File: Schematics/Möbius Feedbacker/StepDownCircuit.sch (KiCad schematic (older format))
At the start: 16 parts

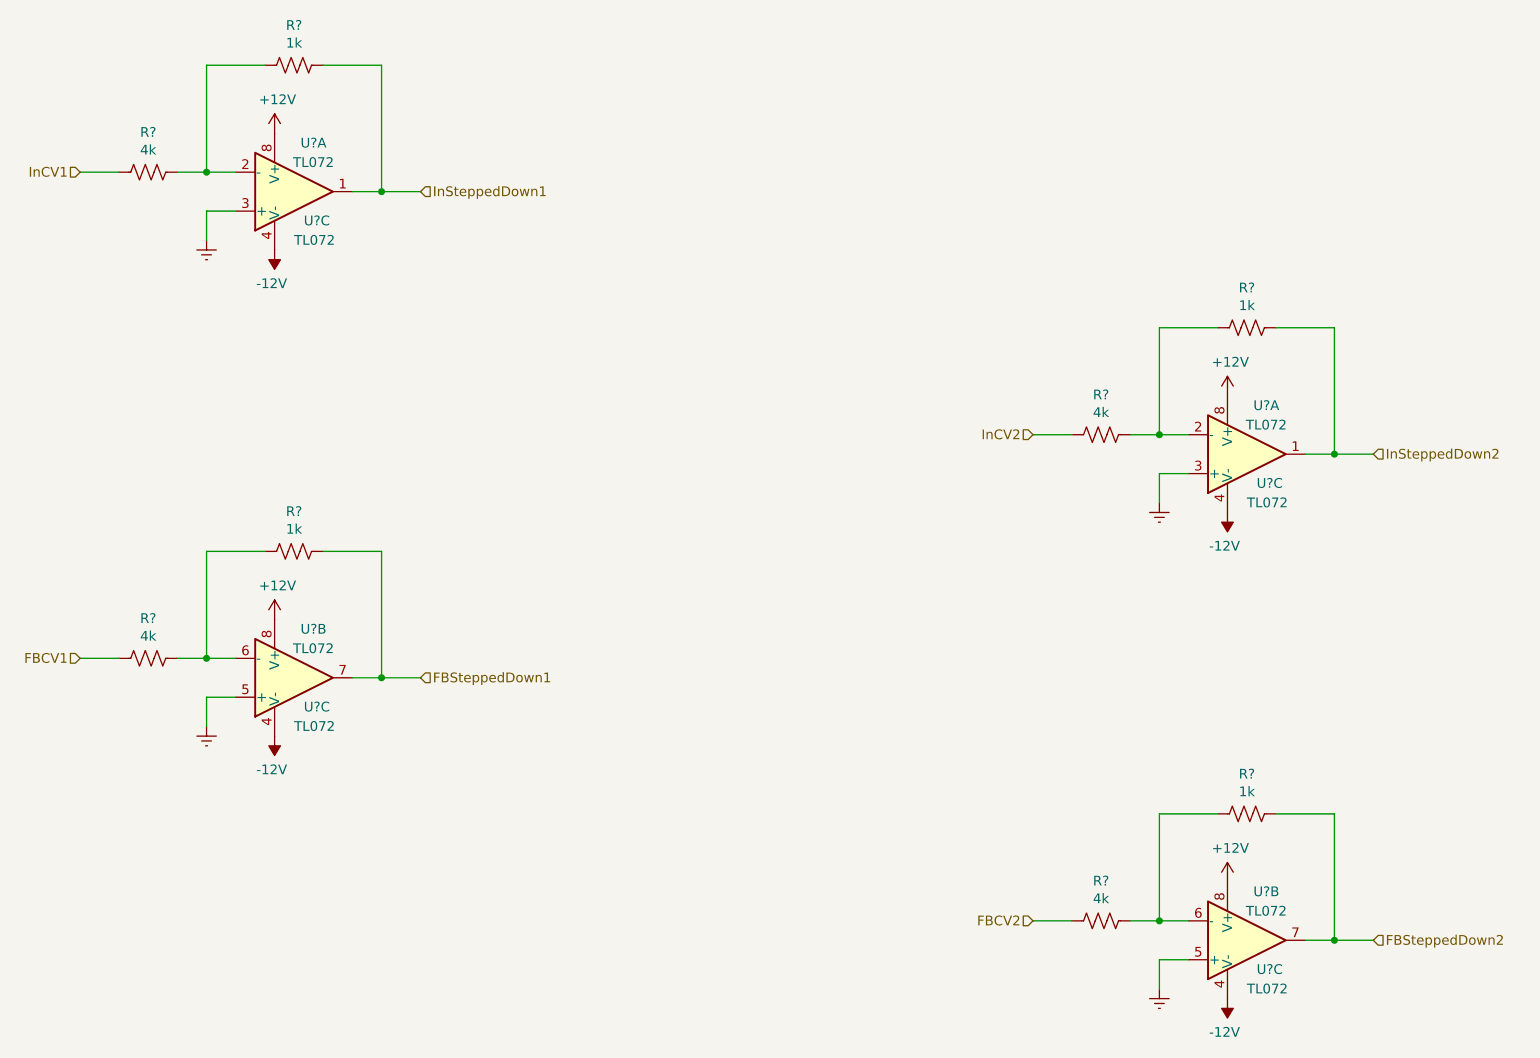
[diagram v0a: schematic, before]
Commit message: Add schematic pdfs, change name to Pathway, update README
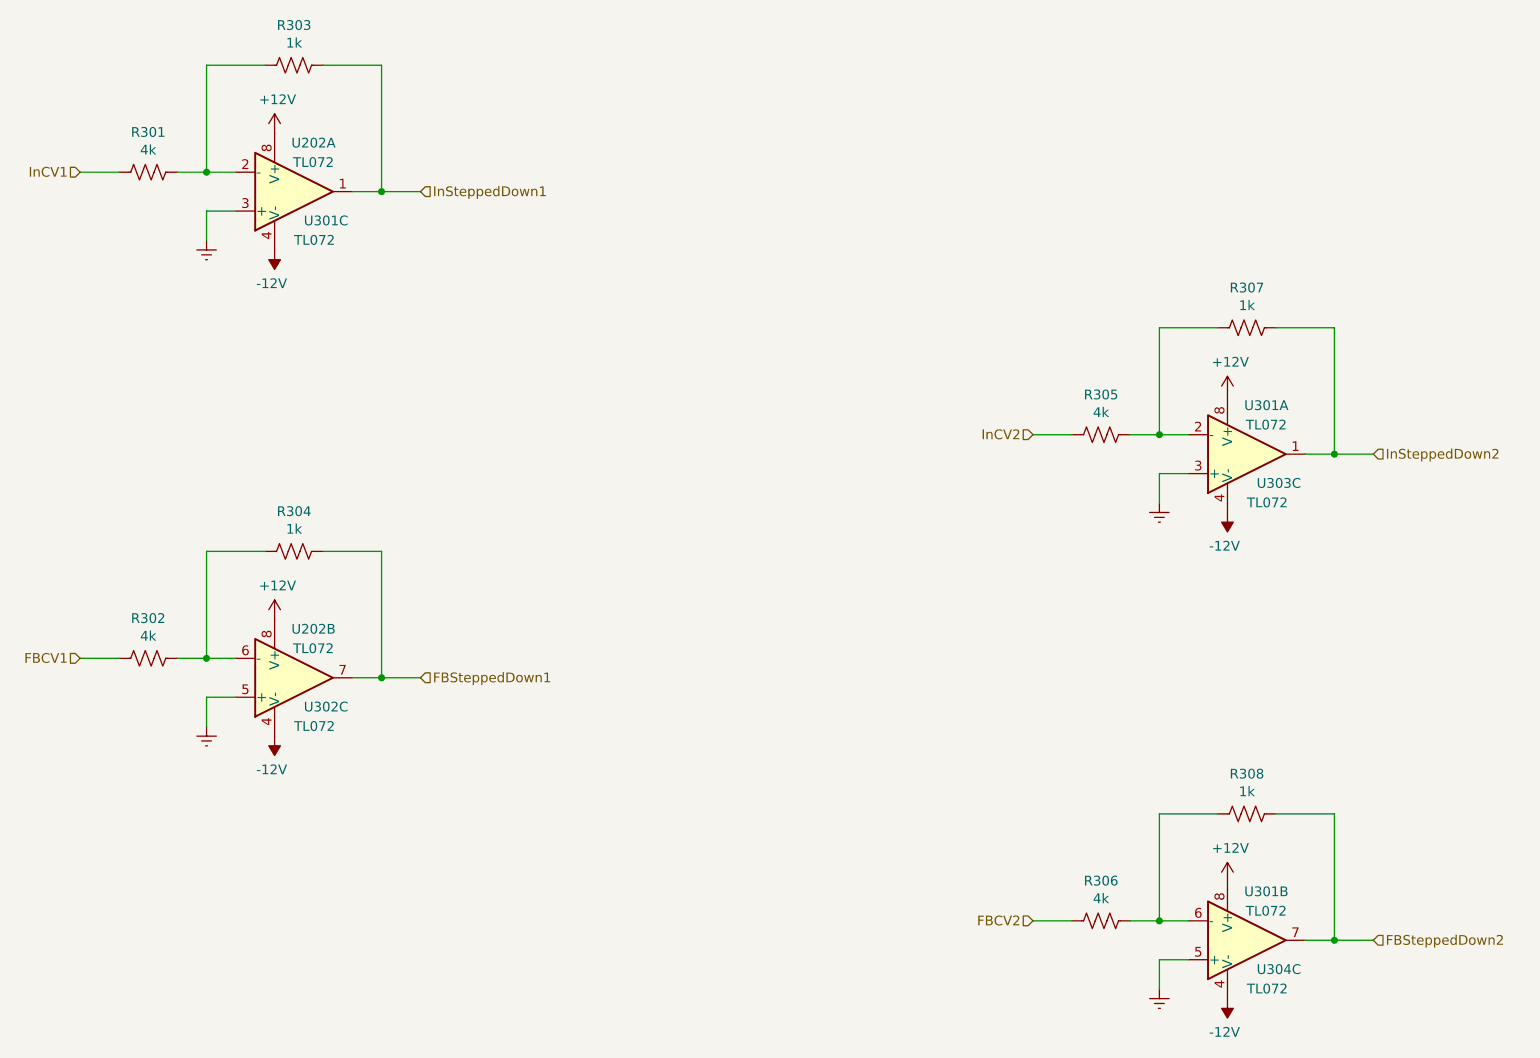
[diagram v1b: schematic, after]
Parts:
- gave numbers to parts that had none: 13
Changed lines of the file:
@@
 $Descr A4 11693 8268
 encoding utf-8
-Sheet 5 4
+Sheet 2 4
 Title ""
 Date ""
@@
 FBSteppedDown1
 $Comp
-L Amplifier_Operational:TL072 U?
+L Amplifier_Operational:TL072 U202
 U 1 1 5E554342
 P 3250 1850
-F 0 "U?" H 3350 1600 50  0000 C CNN
+F 0 "U202" H 3350 1600 50  0000 C CNN
 F 1 "TL072" H 3350 1700 50  0000 C CNN
 F 2 "" H 3250 1850 50  0001 C CNN
@@
 $EndComp
 $Comp
-L Amplifier_Operational:TL072 U?
+L Amplifier_Operational:TL072 U202
 U 2 1 5E5546EC
 P 3250 4350
-F 0 "U?" H 3350 4100 50  0000 C CNN
+F 0 "U202" H 3350 4100 50  0000 C CNN
 F 1 "TL072" H 3350 4200 50  0000 C CNN
 F 2 "" H 3250 4350 50  0001 C CNN
@@
 $EndComp
 $Comp
-L Amplifier_Operational:TL072 U?
+L Amplifier_Operational:TL072 U302
 U 3 1 5E554BFE
 P 3250 4350
-F 0 "U?" H 3300 4200 50  0000 L CNN
+F 0 "U302" H 3300 4200 50  0000 L CNN
 F 1 "TL072" H 3250 4100 50  0000 L CNN
 F 2 "" H 3250 4350 50  0001 C CNN
@@
 $EndComp
 $Comp
-L Amplifier_Operational:TL072 U?
+L Amplifier_Operational:TL072 U301
 U 3 1 5E55AF7D
 P 3250 1850
-F 0 "U?" H 3300 1700 50  0000 L CNN
+F 0 "U301" H 3300 1700 50  0000 L CNN
 F 1 "TL072" H 3250 1600 50  0000 L CNN
 F 2 "" H 3250 1850 50  0001 C CNN
@@
 $EndComp
 $Comp
-L Device:R_US R?
+L Device:R_US R303
 U 1 1 5E56CB01
 P 3250 1200
-F 0 "R?" V 3045 1200 50  0000 C CNN
+F 0 "R303" V 3045 1200 50  0000 C CNN
 F 1 "1k" V 3136 1200 50  0000 C CNN
 F 2 "" V 3290 1190 50  0001 C CNN
@@
 $EndComp
 $Comp
-L Device:R_US R?
+L Device:R_US R301
 U 1 1 5E56D173
 P 2500 1750
-F 0 "R?" V 2295 1750 50  0000 C CNN
+F 0 "R301" V 2295 1750 50  0000 C CNN
 F 1 "4k" V 2386 1750 50  0000 C CNN
 F 2 "" V 2540 1740 50  0001 C CNN
@@
 $EndComp
 $Comp
-L power:Earth #PWR?
+L power:Earth #PWR0301
 U 1 1 5E56D6B1
 P 2800 2100
-F 0 "#PWR?" H 2800 1850 50  0001 C CNN
+F 0 "#PWR0301" H 2800 1850 50  0001 C CNN
 F 1 "Earth" H 2800 1950 50  0001 C CNN
 F 2 "" H 2800 2100 50  0001 C CNN
@@
 $EndComp
 $Comp
-L power:+12V #PWR?
+L power:+12V #PWR0303
 U 1 1 5E56DCE9
 P 3150 1550
-F 0 "#PWR?" H 3150 1400 50  0001 C CNN
+F 0 "#PWR0303" H 3150 1400 50  0001 C CNN
 F 1 "+12V" H 3165 1723 50  0000 C CNN
 F 2 "" H 3150 1550 50  0001 C CNN
@@
 $EndComp
 $Comp
-L power:-12V #PWR?
+L power:-12V #PWR0304
 U 1 1 5E56E042
 P 3150 2150
-F 0 "#PWR?" H 3150 2250 50  0001 C CNN
+F 0 "#PWR0304" H 3150 2250 50  0001 C CNN
 F 1 "-12V" H 3165 2323 50  0000 C CNN
 F 2 "" H 3150 2150 50  0001 C CNN
@@
 	3100 1200 2800 1200
 $Comp
-L Device:R_US R?
+L Device:R_US R304
 U 1 1 5E59192E
 P 3250 3700
-F 0 "R?" V 3045 3700 50  0000 C CNN
+F 0 "R304" V 3045 3700 50  0000 C CNN
 F 1 "1k" V 3136 3700 50  0000 C CNN
 F 2 "" V 3290 3690 50  0001 C CNN
@@
 $EndComp
 $Comp
-L Device:R_US R?
+L Device:R_US R302
 U 1 1 5E591938
 P 2500 4250
-F 0 "R?" V 2295 4250 50  0000 C CNN
+F 0 "R302" V 2295 4250 50  0000 C CNN
 F 1 "4k" V 2386 4250 50  0000 C CNN
 F 2 "" V 2540 4240 50  0001 C CNN
@@
 $EndComp
 $Comp
-L power:Earth #PWR?
+L power:Earth #PWR0302
 U 1 1 5E591942
 P 2800 4600
-F 0 "#PWR?" H 2800 4350 50  0001 C CNN
+F 0 "#PWR0302" H 2800 4350 50  0001 C CNN
 F 1 "Earth" H 2800 4450 50  0001 C CNN
 F 2 "" H 2800 4600 50  0001 C CNN
@@
 $EndComp
 $Comp
-L power:+12V #PWR?
+L power:+12V #PWR0305
 U 1 1 5E59194C
 P 3150 4050
-F 0 "#PWR?" H 3150 3900 50  0001 C CNN
+F 0 "#PWR0305" H 3150 3900 50  0001 C CNN
 F 1 "+12V" H 3165 4223 50  0000 C CNN
 F 2 "" H 3150 4050 50  0001 C CNN
@@
 $EndComp
 $Comp
-L power:-12V #PWR?
+L power:-12V #PWR0306
 U 1 1 5E591956
 P 3150 4650
-F 0 "#PWR?" H 3150 4750 50  0001 C CNN
+F 0 "#PWR0306" H 3150 4750 50  0001 C CNN
 F 1 "-12V" H 3165 4823 50  0000 C CNN
 F 2 "" H 3150 4650 50  0001 C CNN
@@
 FBSteppedDown2
 $Comp
-L Amplifier_Operational:TL072 U?
+L Amplifier_Operational:TL072 U301
 U 1 1 5E5F6235
 P 8150 3200
-F 0 "U?" H 8250 2950 50  0000 C CNN
+F 0 "U301" H 8250 2950 50  0000 C CNN
 F 1 "TL072" H 8250 3050 50  0000 C CNN
 F 2 "" H 8150 3200 50  0001 C CNN
@@
 $EndComp
 $Comp
-L Amplifier_Operational:TL072 U?
+L Amplifier_Operational:TL072 U301
 U 2 1 5E5F623F
 P 8150 5700
-F 0 "U?" H 8250 5450 50  0000 C CNN
+F 0 "U301" H 8250 5450 50  0000 C CNN
 F 1 "TL072" H 8250 5550 50  0000 C CNN
 F 2 "" H 8150 5700 50  0001 C CNN
@@
 $EndComp
 $Comp
-L Amplifier_Operational:TL072 U?
+L Amplifier_Operational:TL072 U304
 U 3 1 5E5F6249
 P 8150 5700
-F 0 "U?" H 8200 5550 50  0000 L CNN
+F 0 "U304" H 8200 5550 50  0000 L CNN
 F 1 "TL072" H 8150 5450 50  0000 L CNN
 F 2 "" H 8150 5700 50  0001 C CNN
@@
 $EndComp
 $Comp
-L Amplifier_Operational:TL072 U?
+L Amplifier_Operational:TL072 U303
 U 3 1 5E5F6253
 P 8150 3200
-F 0 "U?" H 8200 3050 50  0000 L CNN
+F 0 "U303" H 8200 3050 50  0000 L CNN
 F 1 "TL072" H 8150 2950 50  0000 L CNN
 F 2 "" H 8150 3200 50  0001 C CNN
@@
 $EndComp
 $Comp
-L Device:R_US R?
+L Device:R_US R307
 U 1 1 5E5F625D
 P 8150 2550
-F 0 "R?" V 7945 2550 50  0000 C CNN
+F 0 "R307" V 7945 2550 50  0000 C CNN
 F 1 "1k" V 8036 2550 50  0000 C CNN
 F 2 "" V 8190 2540 50  0001 C CNN
@@
 $EndComp
 $Comp
-L Device:R_US R?
+L Device:R_US R305
 U 1 1 5E5F6267
 P 7400 3100
-F 0 "R?" V 7195 3100 50  0000 C CNN
+F 0 "R305" V 7195 3100 50  0000 C CNN
 F 1 "4k" V 7286 3100 50  0000 C CNN
 F 2 "" V 7440 3090 50  0001 C CNN
@@
 $EndComp
 $Comp
-L power:Earth #PWR?
+L power:Earth #PWR0307
 U 1 1 5E5F6271
 P 7700 3450
-F 0 "#PWR?" H 7700 3200 50  0001 C CNN
+F 0 "#PWR0307" H 7700 3200 50  0001 C CNN
 F 1 "Earth" H 7700 3300 50  0001 C CNN
 F 2 "" H 7700 3450 50  0001 C CNN
@@
 $EndComp
 $Comp
-L power:+12V #PWR?
+L power:+12V #PWR0309
 U 1 1 5E5F627B
 P 8050 2900
-F 0 "#PWR?" H 8050 2750 50  0001 C CNN
+F 0 "#PWR0309" H 8050 2750 50  0001 C CNN
 F 1 "+12V" H 8065 3073 50  0000 C CNN
 F 2 "" H 8050 2900 50  0001 C CNN
@@
 $EndComp
 $Comp
-L power:-12V #PWR?
+L power:-12V #PWR0310
 U 1 1 5E5F6285
 P 8050 3500
-F 0 "#PWR?" H 8050 3600 50  0001 C CNN
+F 0 "#PWR0310" H 8050 3600 50  0001 C CNN
 F 1 "-12V" H 8065 3673 50  0000 C CNN
 F 2 "" H 8050 3500 50  0001 C CNN
@@
 	8000 2550 7700 2550
 $Comp
-L Device:R_US R?
+L Device:R_US R308
 U 1 1 5E5F629C
 P 8150 5050
-F 0 "R?" V 7945 5050 50  0000 C CNN
+F 0 "R308" V 7945 5050 50  0000 C CNN
 F 1 "1k" V 8036 5050 50  0000 C CNN
 F 2 "" V 8190 5040 50  0001 C CNN
@@
 $EndComp
 $Comp
-L Device:R_US R?
+L Device:R_US R306
 U 1 1 5E5F62A6
 P 7400 5600
-F 0 "R?" V 7195 5600 50  0000 C CNN
+F 0 "R306" V 7195 5600 50  0000 C CNN
 F 1 "4k" V 7286 5600 50  0000 C CNN
 F 2 "" V 7440 5590 50  0001 C CNN
@@
 $EndComp
 $Comp
-L power:Earth #PWR?
+L power:Earth #PWR0308
 U 1 1 5E5F62B0
 P 7700 5950
-F 0 "#PWR?" H 7700 5700 50  0001 C CNN
+F 0 "#PWR0308" H 7700 5700 50  0001 C CNN
 F 1 "Earth" H 7700 5800 50  0001 C CNN
 F 2 "" H 7700 5950 50  0001 C CNN
@@
 $EndComp
 $Comp
-L power:+12V #PWR?
+L power:+12V #PWR0311
 U 1 1 5E5F62BA
 P 8050 5400
-F 0 "#PWR?" H 8050 5250 50  0001 C CNN
+F 0 "#PWR0311" H 8050 5250 50  0001 C CNN
 F 1 "+12V" H 8065 5573 50  0000 C CNN
 F 2 "" H 8050 5400 50  0001 C CNN
@@
 $EndComp
 $Comp
-L power:-12V #PWR?
+L power:-12V #PWR0312
 U 1 1 5E5F62C4
 P 8050 6000
-F 0 "#PWR?" H 8050 6100 50  0001 C CNN
+F 0 "#PWR0312" H 8050 6100 50  0001 C CNN
 F 1 "-12V" H 8065 6173 50  0000 C CNN
 F 2 "" H 8050 6000 50  0001 C CNN
